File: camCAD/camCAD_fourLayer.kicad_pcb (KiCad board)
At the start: 2 copper layers, 98.9 x 55.2 mm, 70 parts, among them J1 USB C Charging Port, J2 JTAG header, J3 BATTERY, J4 ILI9341_Display_Header, SW1 NRST_SW, SW2 Pictures/Back, SW3 Forward, SW4 Backward, SW5 Flash/Delete, SW6 Shutter, U1 BQ24072RGTR Charging IC, U2 SC189ZSKTRT, U3 STM32F407ZGTx, U4 AP3602AKTR-G1 Charge Pump, U5 Flash LED, U6 ADA 254

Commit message: Starting 4 layer layout
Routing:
- net SC_3V3: track 351.7 -> 1.88 mm, vias 17 -> 0
- net BATT-: track 258.0 -> 3.88 mm, vias 19 -> 0
- net BATT+: track 142.4 -> 0.00 mm, vias 2 -> 0
- net /STM32_Power_Requirements/CapJunction: track 120.1 -> 0.00 mm, vias 12 -> 0
- net PG5: track 74.8 -> 0.00 mm, vias 1 -> 0
- net BQ_OUT: track 62.8 -> 0.00 mm, vias 2 -> 0
- net NRST: track 57.9 -> 0.00 mm, vias 2 -> 0
- net PG4: track 53.1 -> 0.00 mm
- net BQ_IN: track 53.1 -> 0.00 mm, vias 2 -> 0
- net PG1: track 52.9 -> 0.00 mm, vias 2 -> 0
- net PA5: track 51.4 -> 0.00 mm, vias 2 -> 0
- net PA9: track 51.2 -> 0.00 mm, vias 2 -> 0
- net PG3: track 50.2 -> 0.00 mm
- net PA8: track 49.7 -> 0.00 mm, vias 2 -> 0
- net PG2: track 46.8 -> 0.00 mm, vias 2 -> 0
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- removed copper zone on B.Cu, net BATT-
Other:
- board outline removed

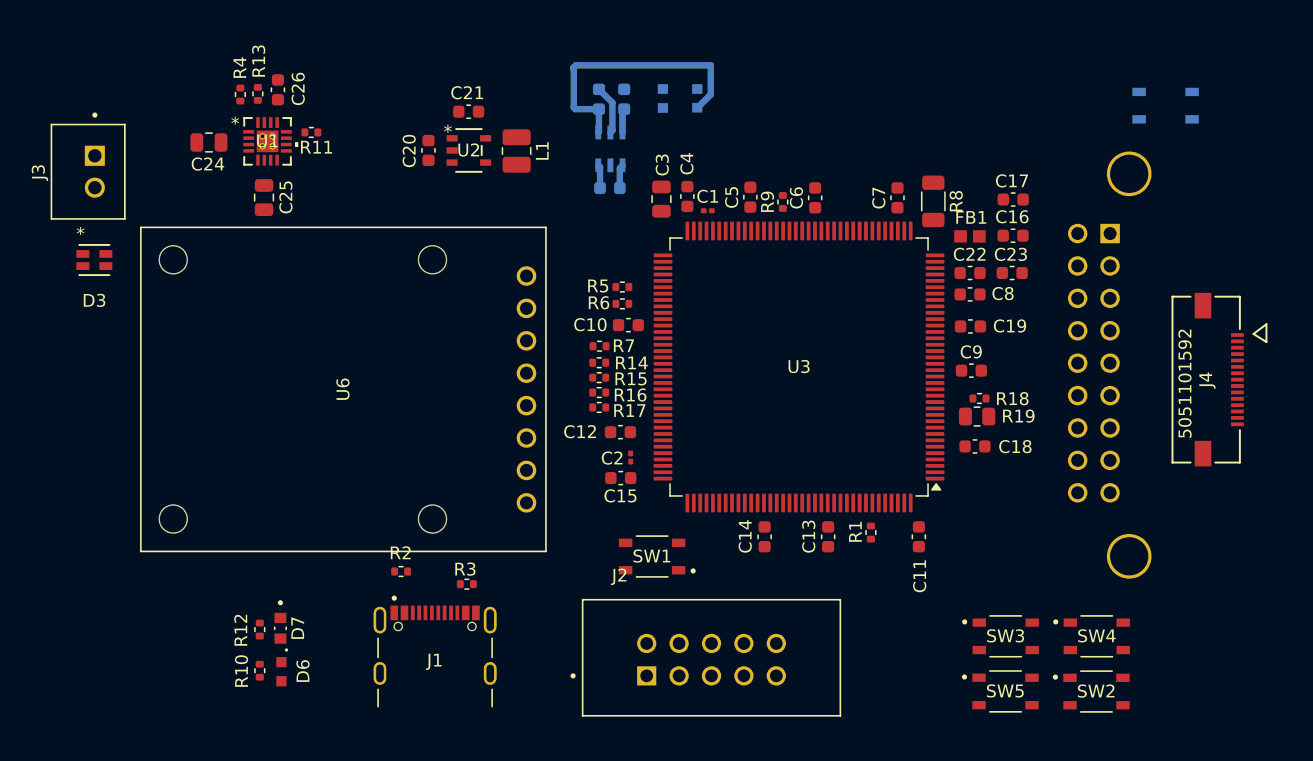
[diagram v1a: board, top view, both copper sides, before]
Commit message: Made some progress on four layers
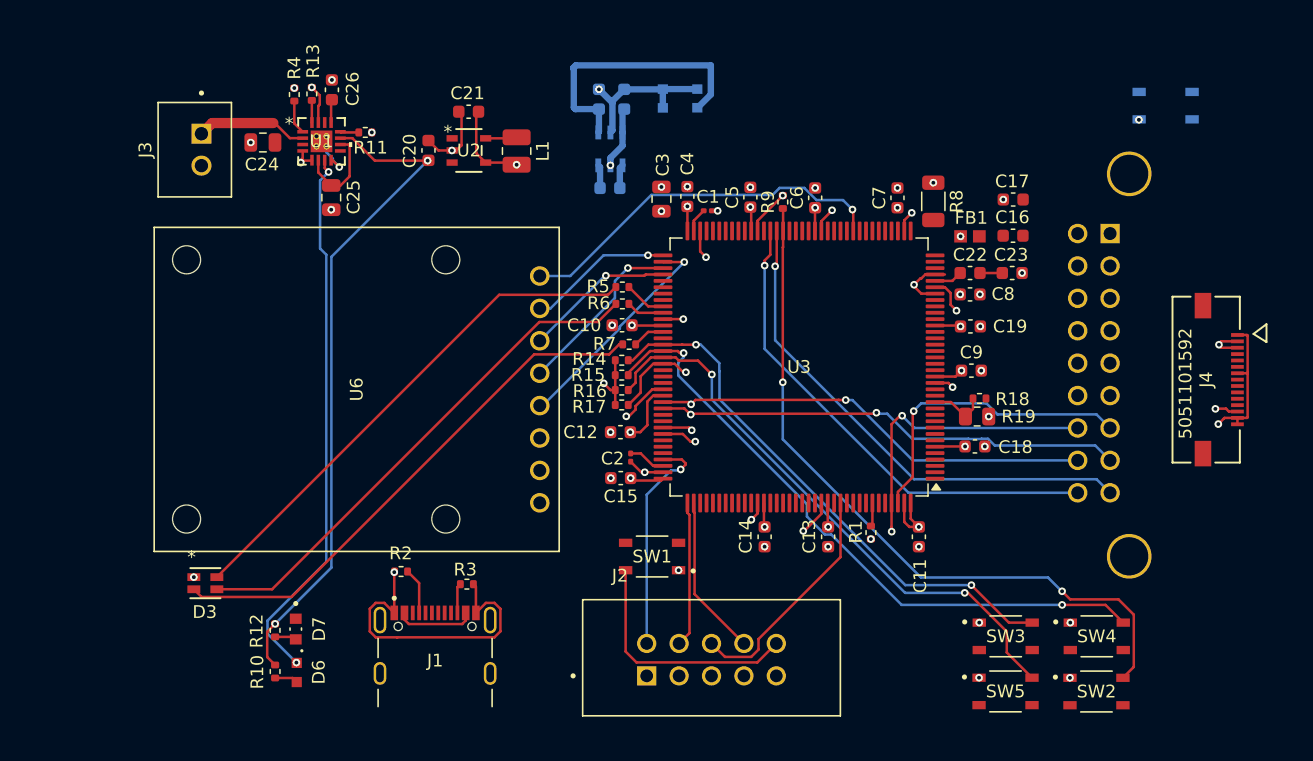
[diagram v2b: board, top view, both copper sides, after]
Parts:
- moved D3 26.8 mm to (83.0, 90.3)
- moved J3 8.53 mm to (82.2, 56.3)
- moved C25 5.27 mm to (92.9, 60.1)
- moved C24 4.23 mm to (87.5, 55.8)
- moved R11 4.23 mm to (95.5, 55.0)
- moved R13 4.23 mm to (91.3, 51.9)
- moved R4 4.23 mm to (90.0, 52.0)
- moved U1 4.23 mm to (92.1, 55.7)
- moved C26 4.23 mm to (92.9, 51.6)
- moved R7 2.33 mm to (116.2, 71.6)
- moved R14 1.78 mm to (115.6, 72.8)
- moved R15 1.78 mm to (115.6, 74.0)
- moved R16 1.78 mm to (115.6, 75.2)
- moved R17 1.78 mm to (115.6, 76.3)
- moved R10 1.20 mm to (88.5, 97.2)
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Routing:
- net /STM32_Power_Requirements/CapJunction: track 0.00 -> 91.0 mm, vias 0 -> 13
- net BATT-: track 3.88 -> 91.4 mm, vias 0 -> 32
- net PG1: track 0.00 -> 56.6 mm, vias 0 -> 2
- net BQ_OUT: track 0.00 -> 52.6 mm, vias 0 -> 2
- net PG3: track 0.00 -> 50.7 mm, vias 0 -> 2
- net SC_3V3: track 1.88 -> 50.8 mm, vias 0 -> 26
- net PG4: track 0.00 -> 45.7 mm, vias 0 -> 2
- net PG2: track 0.00 -> 42.8 mm, vias 0 -> 2
- net BQ_PGOOD: track 0.00 -> 42.8 mm, vias 0 -> 2
- net Net-(D3-R): track 0.00 -> 42.1 mm
- net Net-(D3-B): track 0.00 -> 40.7 mm
- net Net-(D3-G): track 0.00 -> 40.5 mm
- net PE7: track 0.00 -> 39.8 mm, vias 0 -> 1
- net PE8: track 0.00 -> 38.6 mm, vias 0 -> 1
- net PC7: track 0.00 -> 36.9 mm, vias 0 -> 2
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- added copper zone on In2.Cu, net BATT-
- added copper zone on In1.Cu, net SC_3V3
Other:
- copper layers 2 -> 4

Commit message: Completed first draft of four layer, updated layout readme
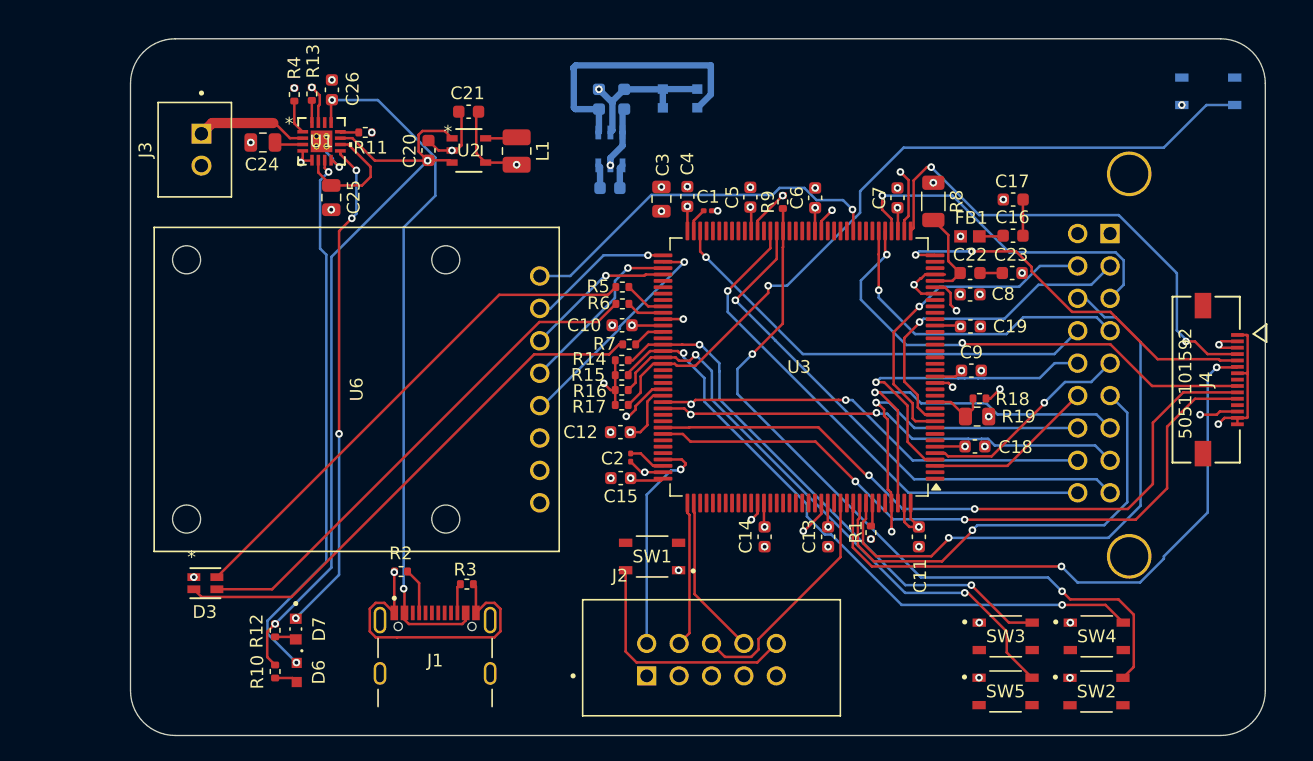
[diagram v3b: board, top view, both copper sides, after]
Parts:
- moved SW6 3.53 mm to (161.6, 51.7)
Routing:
- net BATT+: track 8.77 -> 81.6 mm, vias 0 -> 1
- net PG5: track 6.87 -> 59.5 mm
- net PA8: track 2.34 -> 54.3 mm, vias 1 -> 2
- net PA9: track 2.78 -> 54.6 mm, vias 1 -> 2
- net PB5: track 0.00 -> 48.1 mm, vias 0 -> 2
- net BQ_IN: track 8.00 -> 54.7 mm, vias 0 -> 2
- net PB7: track 0.00 -> 46.3 mm, vias 0 -> 1
- net BQ_CHG: track 0.00 -> 39.2 mm, vias 0 -> 4
- net PA5: track 0.00 -> 38.7 mm, vias 0 -> 2
- net PA3: track 0.00 -> 38.7 mm, vias 0 -> 2
- net NRST: track 21.2 -> 59.7 mm
- net PB6: track 0.00 -> 35.9 mm, vias 0 -> 1
- net PB11: track 2.25 -> 35.3 mm
- net PA2: track 0.00 -> 30.6 mm, vias 0 -> 2
- net PA4: track 0.00 -> 27.5 mm, vias 0 -> 1
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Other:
- board outline added: 89 x 54.6 mm
